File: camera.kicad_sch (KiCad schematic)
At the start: 1 part, among them J10 Conn_01x24_MountingPin

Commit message: Layout SDRAM
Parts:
- J10: footprint (none) -> Connector_FFC-FPC:Hirose_FH12-24S-0.5SH_1x24-1MP_P0.50mm_Horizontal
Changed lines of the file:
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@@
 			)
 		)
-		(property "Footprint" ""
+		(property "Footprint" "Connector_FFC-FPC:Hirose_FH12-24S-0.5SH_1x24-1MP_P0.50mm_Horizontal"
 			(at 215.9 102.87 0)
 			(effects

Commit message: Finished SDRAM, QSPI Flash, Planning to move to 5 inch orient display dimension
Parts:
- J10: JLCPCB Part # (none) -> C262683
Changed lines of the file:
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@@
+			)
+		)
+		(property "JLCPCB Part #" "C262683"
+			(at 215.9 102.87 0)
+			(effects
+				(font
+					(size 1.27 1.27)
+				)
+				(hide yes)
 			)
 		)

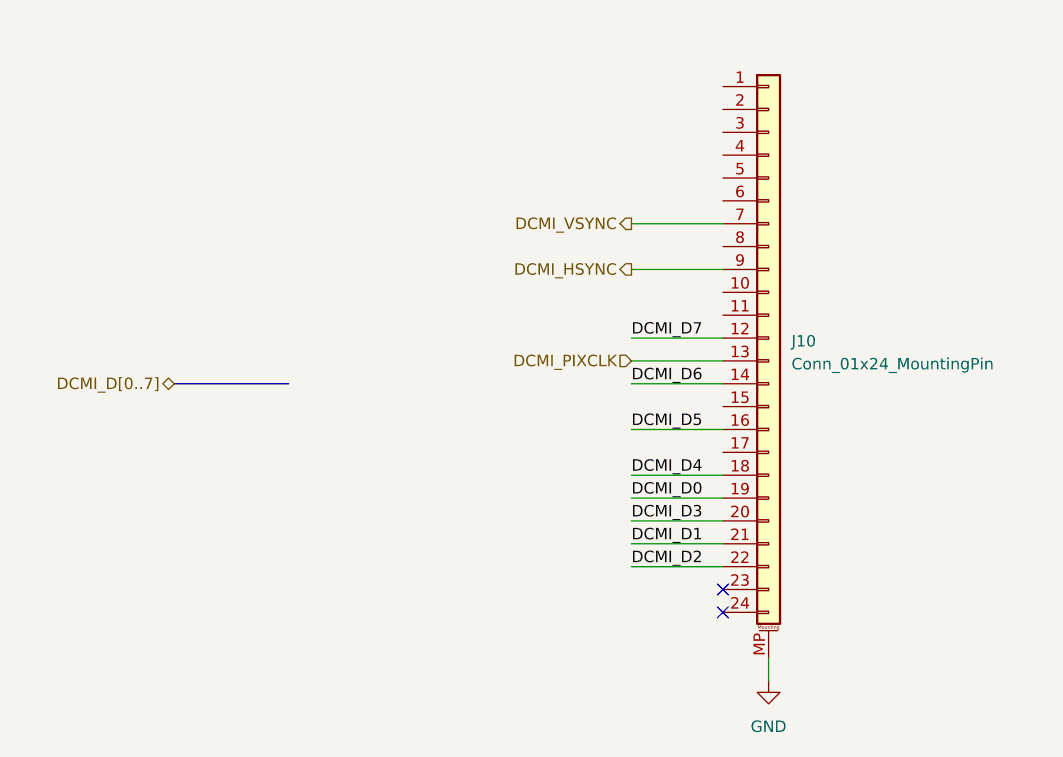
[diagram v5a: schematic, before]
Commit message: Button, LED, i2s audio, LCD & SD ctrl left
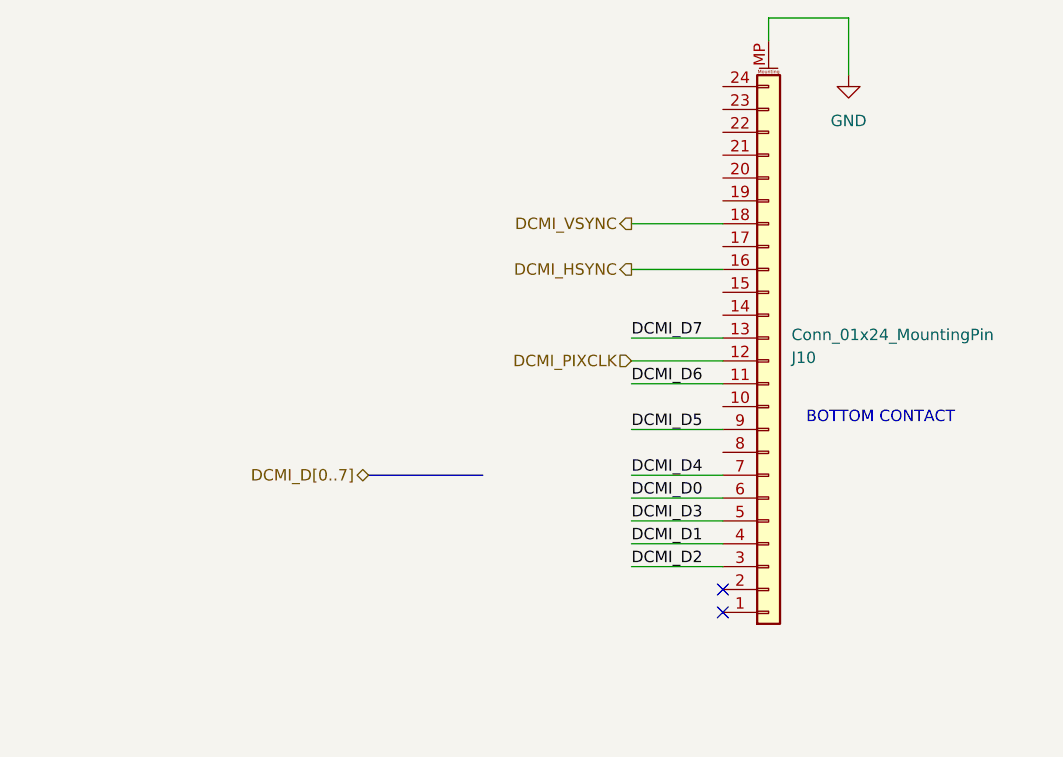
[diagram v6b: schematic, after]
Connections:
- net DCMI_D0: now also J10.6 (Pin_6); no longer J10.19 (Pin_19)
- net DCMI_D1: now also J10.4 (Pin_4); no longer J10.21 (Pin_21)
- net DCMI_D2: now also J10.3 (Pin_3); no longer J10.22 (Pin_22)
- net DCMI_D3: now also J10.5 (Pin_5); no longer J10.20 (Pin_20)
- net DCMI_D4: now also J10.7 (Pin_7); no longer J10.18 (Pin_18)
- net DCMI_D5: now also J10.9 (Pin_9); no longer J10.16 (Pin_16)
- net DCMI_D6: now also J10.11 (Pin_11); no longer J10.14 (Pin_14)
- net DCMI_D7: now also J10.13 (Pin_13); no longer J10.12 (Pin_12)
- net DCMI_HSYNC: now also J10.16 (Pin_16); no longer J10.9 (Pin_9)
- net DCMI_PIXCLK: now also J10.12 (Pin_12); no longer J10.13 (Pin_13)
- net DCMI_VSYNC: now also J10.18 (Pin_18); no longer J10.7 (Pin_7)
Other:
- note added: "BOTTOM CONTACT"
- moved on the sheet: J10
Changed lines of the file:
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@@
 	(wire
 		(pts
+			(xy 224.79 67.31) (xy 215.9 67.31)
+		)
+		(stroke
+			(width 0)
+			(type default)
+		)
+	)
+	(wire
+		(pts
 			(xy 200.66 113.03) (xy 210.82 113.03)
 		)
@@
 	(bus
 		(pts
-			(xy 149.86 107.95) (xy 162.56 107.95)
+			(xy 171.45 118.11) (xy 184.15 118.11)
 		)
 		(stroke
@@
 	(wire
 		(pts
-			(xy 215.9 140.97) (xy 215.9 138.43)
+			(xy 224.79 67.31) (xy 224.79 73.66)
 		)
 		(stroke
@@
 	(wire
 		(pts
+			(xy 215.9 67.31) (xy 215.9 69.85)
+		)
+		(stroke
+			(width 0)
+			(type default)
+		)
+	)
+	(wire
+		(pts
 			(xy 200.66 123.19) (xy 210.82 123.19)
 		)
@@
 		)
 	)
+	(text "BOTTOM CONTACT"
+		(exclude_from_sim no)
+		(at 228.346 111.76 0)
+		(effects
+			(font
+				(size 1.27 1.27)
+			)
+		)
+	)
 	(label "DCMI_D6"
 		(at 200.66 107.95 0)
@@
 	(hierarchical_label "DCMI_D[0..7]"
 		(shape bidirectional)
-		(at 149.86 107.95 180)
+		(at 171.45 118.11 180)
 		(fields_autoplaced yes)
 		(effects
@@
 	(symbol
 		(lib_id "power:GND")
-		(at 215.9 140.97 0)
+		(at 224.79 73.66 0)
 		(unit 1)
 		(exclude_from_sim no)
@@
 		(fields_autoplaced yes)
 		(property "Reference" "#PWR051"
-			(at 215.9 147.32 0)
+			(at 224.79 80.01 0)
 			(effects
 				(font
@@
 		)
 		(property "Value" "GND"
-			(at 215.9 146.05 0)
+			(at 224.79 78.74 0)
 			(effects
 				(font
@@
 		)
 		(property "Footprint" ""
-			(at 215.9 140.97 0)
+			(at 224.79 73.66 0)
 			(effects
 				(font
@@
 		)
 		(property "Datasheet" ""
-			(at 215.9 140.97 0)
+			(at 224.79 73.66 0)
 			(effects
 				(font
@@
 		)
 		(property "Description" "Power symbol creates a global label with name \"GND\" , ground"
-			(at 215.9 140.97 0)
+			(at 224.79 73.66 0)
 			(effects
 				(font
@@
 	(symbol
 		(lib_id "Connector_Generic_MountingPin:Conn_01x24_MountingPin")
-		(at 215.9 102.87 0)
+		(at 215.9 105.41 0)
+		(mirror x)
 		(unit 1)
 		(exclude_from_sim no)
@@
 		(on_board yes)
 		(dnp no)
-		(fields_autoplaced yes)
 		(property "Reference" "J10"
-			(at 218.44 103.2255 0)
+			(at 218.44 105.0545 0)
 			(effects
 				(font
@@
 		)
 		(property "Value" "Conn_01x24_MountingPin"
-			(at 218.44 105.7655 0)
+			(at 218.44 102.5145 0)
 			(effects
 				(font
@@
 		)
 		(property "Footprint" "Connector_FFC-FPC:Hirose_FH12-24S-0.5SH_1x24-1MP_P0.50mm_Horizontal"
-			(at 215.9 102.87 0)
+			(at 215.9 105.41 0)
 			(effects
 				(font
@@
 		)
 		(property "Datasheet" "~"
-			(at 215.9 102.87 0)
+			(at 215.9 105.41 0)
 			(effects
 				(font
@@
 		)
 		(property "Description" "Generic connectable mounting pin connector, single row, 01x24, script generated (kicad-library-utils/schlib/autogen/connector/)"
-			(at 215.9 102.87 0)
+			(at 215.9 105.41 0)
 			(effects
 				(font
@@
 		)
 		(property "JLCPCB Part #" "C262683"
-			(at 215.9 102.87 0)
+			(at 215.9 105.41 0)
 			(effects
 				(font

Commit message: Still on progress...
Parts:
- J10: footprint Connector_FFC-FPC:Hirose_FH12-24S-0.5SH_1x24-1MP_P0.50mm_Horizontal -> Connector_FFC-FPC:Jushuo_AFC07-S24FCA-00_1x24-1MP_P0.50_Horizontal; JLCPCB Part # C262683 -> C262567
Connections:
- net CAM_SCL: now reaches J10.20 (Pin_20)
- net CAM_SDA: now reaches J10.22 (Pin_22)
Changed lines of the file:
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@@
 	(wire
 		(pts
+			(xy 200.66 80.01) (xy 210.82 80.01)
+		)
+		(stroke
+			(width 0)
+			(type default)
+		)
+	)
+	(wire
+		(pts
+			(xy 200.66 85.09) (xy 210.82 85.09)
+		)
+		(stroke
+			(width 0)
+			(type default)
+		)
+	)
+	(wire
+		(pts
 			(xy 200.66 125.73) (xy 210.82 125.73)
 		)
@@
 		)
 	)
+	(hierarchical_label "CAM_SCL"
+		(shape input)
+		(at 200.66 85.09 180)
+		(fields_autoplaced yes)
+		(effects
+			(font
+				(size 1.27 1.27)
+			)
+			(justify right)
+		)
+	)
 	(hierarchical_label "DCMI_HSYNC"
 		(shape output)
@@
 		)
 	)
+	(hierarchical_label "CAM_SDA"
+		(shape bidirectional)
+		(at 200.66 80.01 180)
+		(fields_autoplaced yes)
+		(effects
+			(font
+				(size 1.27 1.27)
+			)
+			(justify right)
+		)
+	)
 	(hierarchical_label "DCMI_VSYNC"
 		(shape output)
@@
 			)
 		)
-		(property "Footprint" "Connector_FFC-FPC:Hirose_FH12-24S-0.5SH_1x24-1MP_P0.50mm_Horizontal"
+		(property "Footprint" "Connector_FFC-FPC:Jushuo_AFC07-S24FCA-00_1x24-1MP_P0.50_Horizontal"
 			(at 215.9 105.41 0)
 			(effects
@@
 			)
 		)
-		(property "JLCPCB Part #" "C262683"
+		(property "JLCPCB Part #" "C262567"
 			(at 215.9 105.41 0)
 			(effects
